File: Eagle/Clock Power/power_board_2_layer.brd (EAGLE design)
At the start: 21 parts

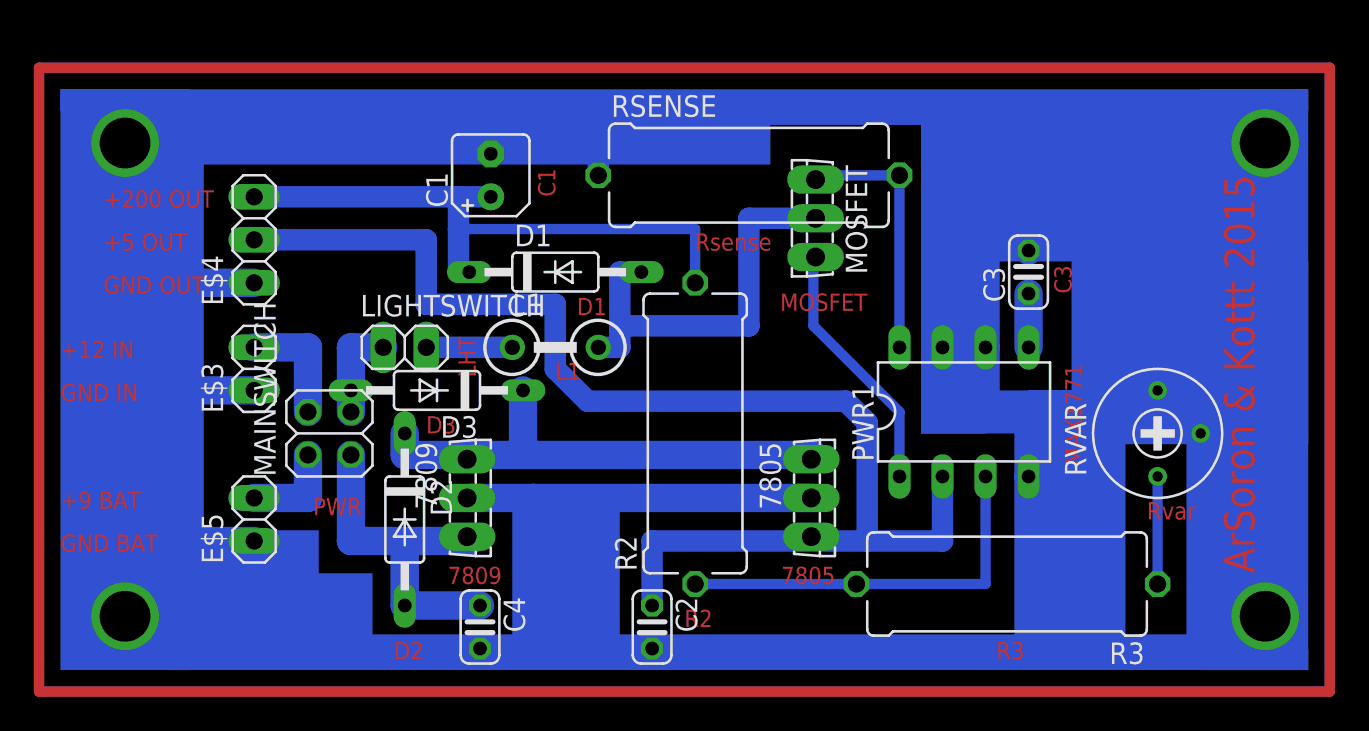
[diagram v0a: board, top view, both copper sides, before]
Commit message: 2 layered board update
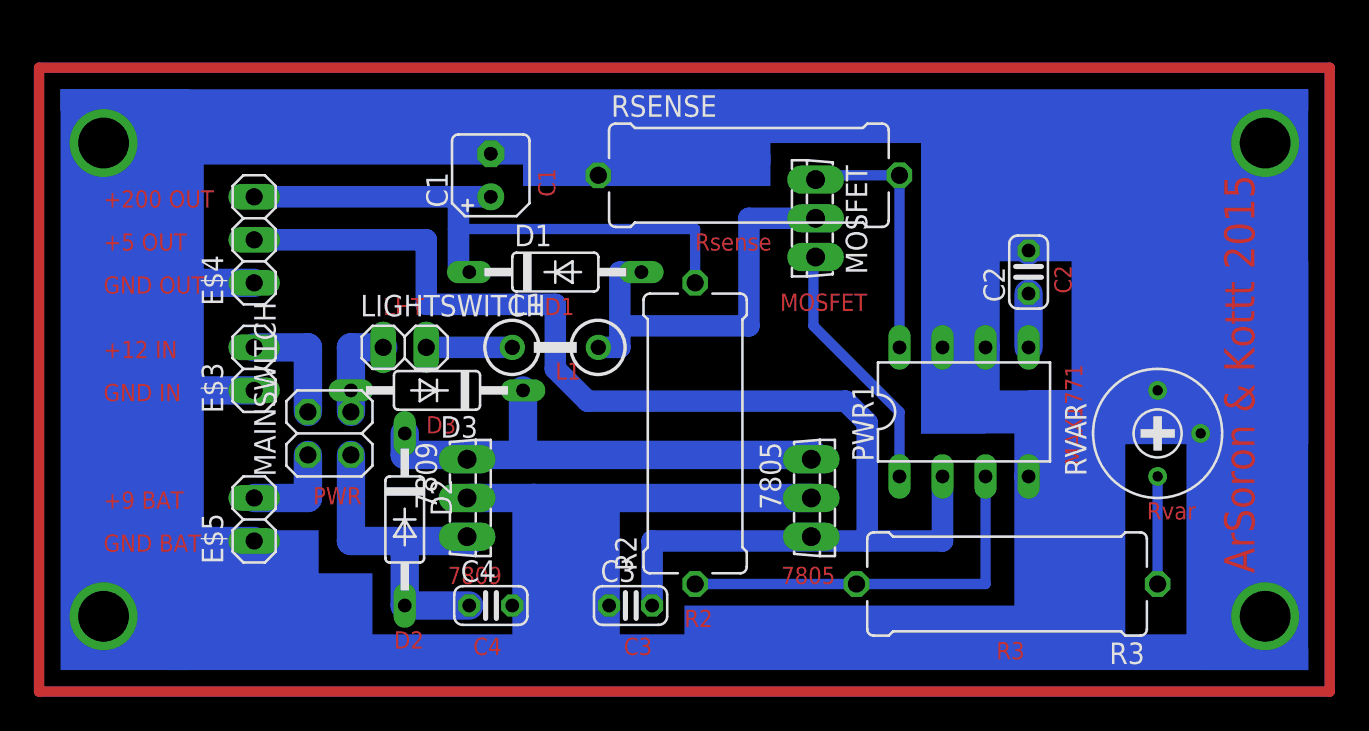
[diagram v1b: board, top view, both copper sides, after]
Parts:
- moved C3 30.7 mm to (19.7, 41.9), turned to 0 degrees
- moved C2 30.5 mm to (43.2, 61.6), turned to 90 degrees
- moved C4 1.42 mm to (11.4, 41.9), turned to 0 degrees
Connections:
- net S$2: now also C2.1; no longer C3.1
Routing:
- net S$18: track 4.45 -> 3.81 mm
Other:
- board text added: "C2"
- board text added: "C4"
